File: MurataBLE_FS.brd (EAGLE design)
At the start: 90 x 63 mm, 48 parts, among them CON2 C-2395.microSD, IC1 74LVC1G00DBV, IC2 IC_DCDC_LM27313, IC3 IC_LPC11U3XQFN33, IC4 IC_LDO_XX1117_4, IC5 1265-1139-1-ND, Q1 CLOCK_CRYSTAL_4_3225, SW1 SW_TACTSW_2PP8073, SW2 SW_TACTSW_2PP8073, SW3 SW_TACTSW_2PP8073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

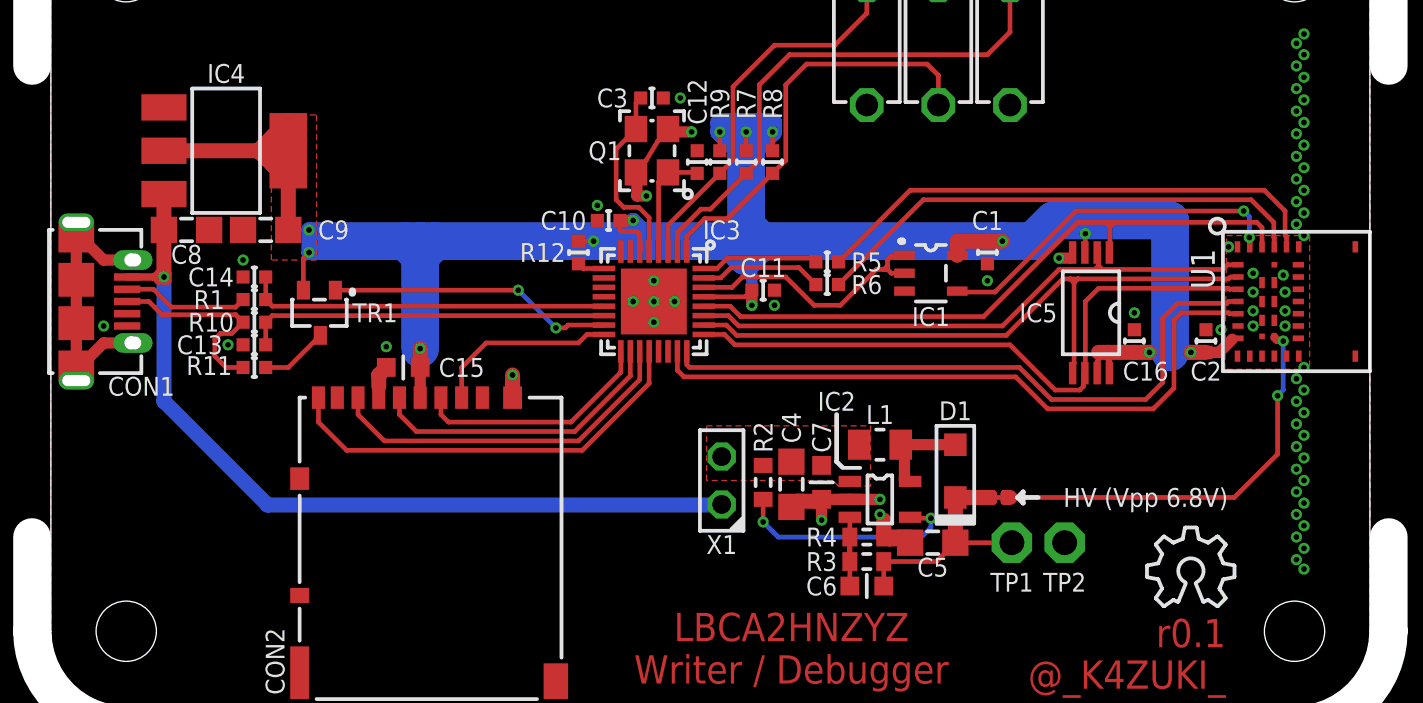
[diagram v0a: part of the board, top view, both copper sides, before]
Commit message: [ FS ] add LED1/R13/R14
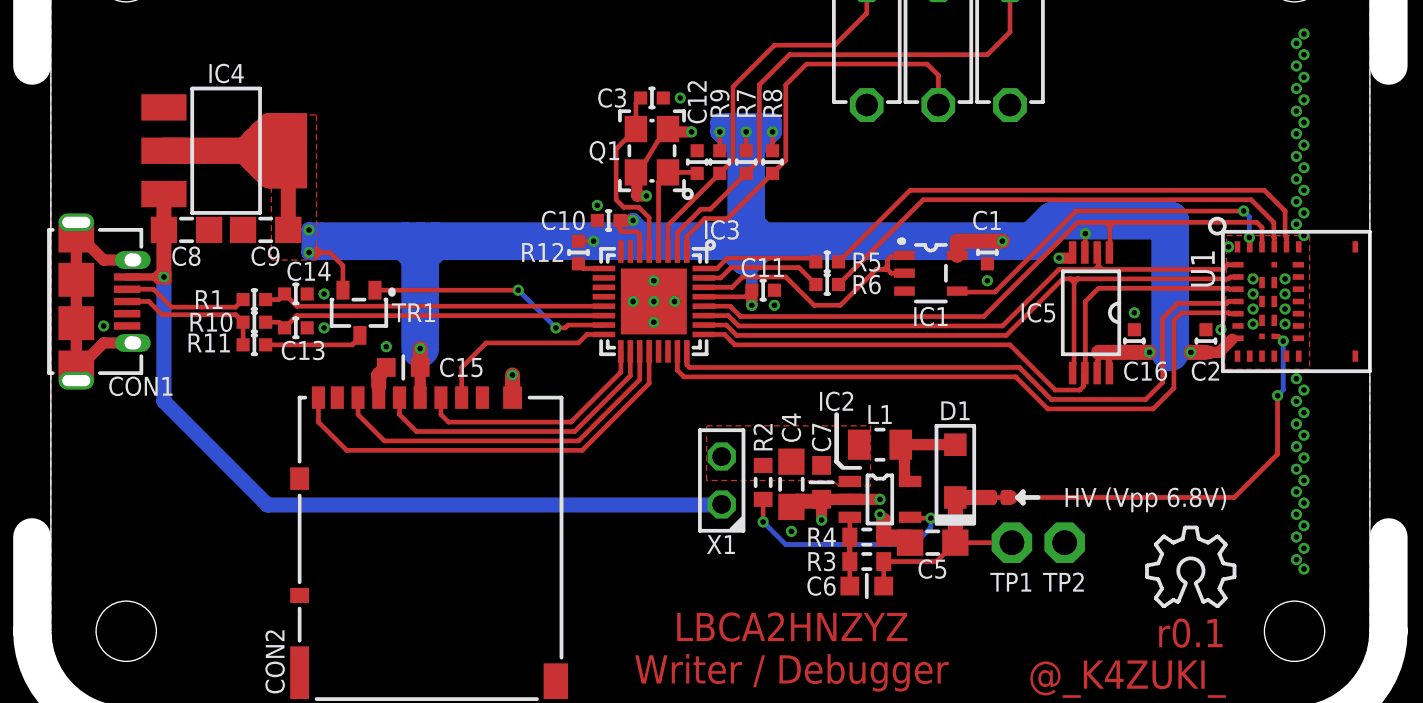
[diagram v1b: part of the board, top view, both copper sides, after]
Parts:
- moved C13 2.38 mm to (23.0, 30.1), turned to 0 degrees
- moved C14 2.38 mm to (23.0, 31.9), turned to 0 degrees
- moved TR1 2.10 mm to (26.4, 30.9)
- moved R11 1.20 mm to (20.8, 29.2)
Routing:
- net D+: track 11.1 -> 7.81 mm
- net N$12: track 15.1 -> 13.0 mm
- net N$2: track 3.60 -> 5.27 mm
- net N$20: track 19.3 -> 18.3 mm
- net N$24: track 19.3 -> 18.3 mm

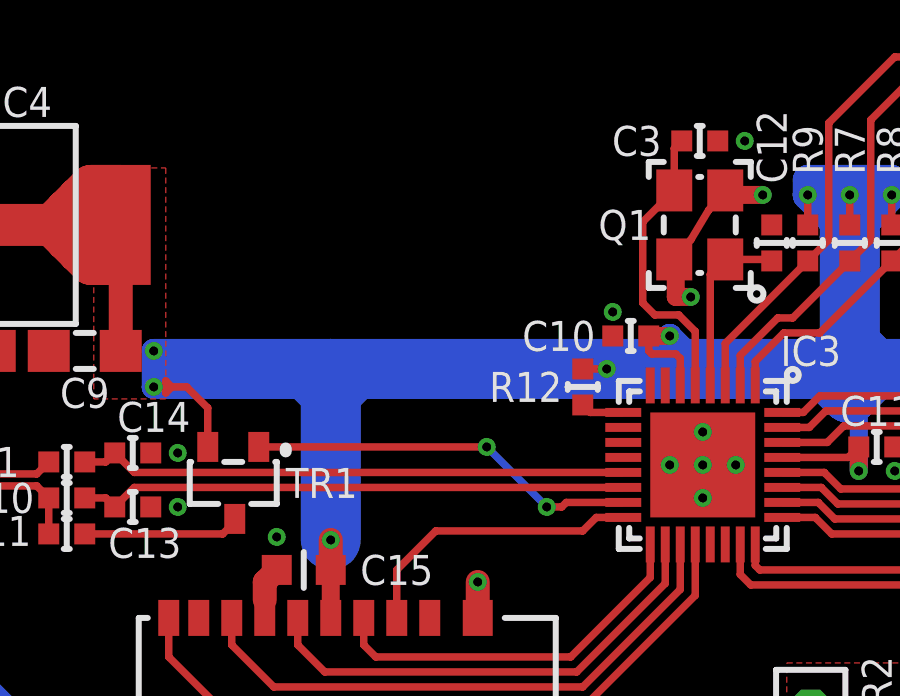
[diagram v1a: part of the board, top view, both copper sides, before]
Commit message: [ FS ] add LED1/R13/R14
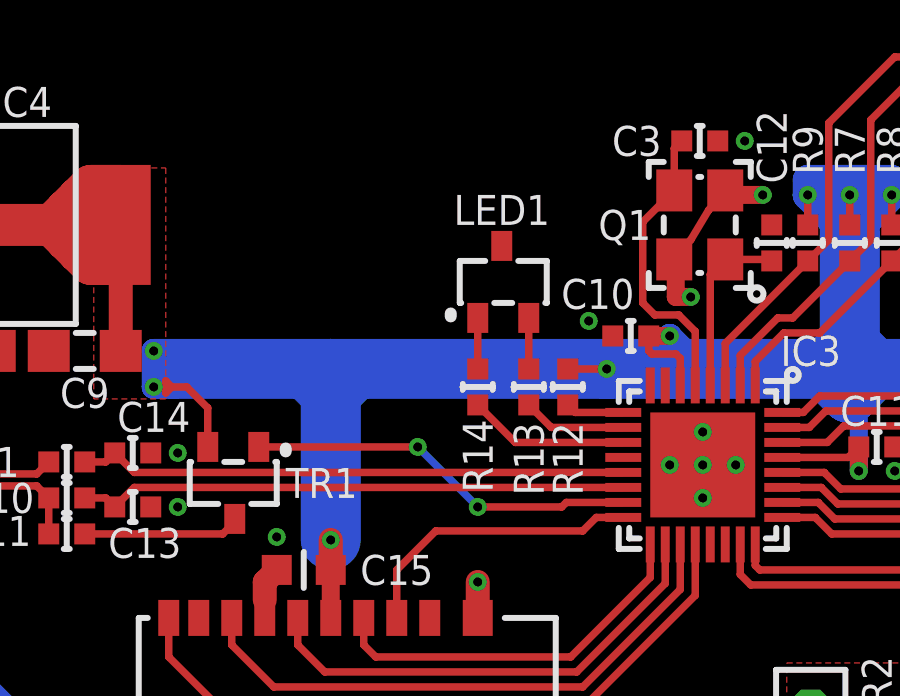
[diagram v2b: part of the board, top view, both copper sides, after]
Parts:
- added LED1: (no value), mylib:SOT95P300X140-3N
- added R13, R14: 100/1005, mylib:C0402
- moved R12 0.50 mm to (37.5, 34.1)
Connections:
- new net N$14: LED1.1, R14.2
- new net N$3: IC3.10, R13.1
- new net N$6: IC3.11, R14.1
- new net N$9: LED1.2, R13.2
- net GND: now also LED1.3
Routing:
- net N$6: track 0.00 -> 5.37 mm
- net N$3: track 0.00 -> 3.46 mm
- net N$9: track 0.00 -> 1.70 mm
- net N$14: track 0.00 -> 1.70 mm
- net N$13: track 1.45 -> 1.95 mm
- net 3.3V: track 145.4 -> 145.9 mm
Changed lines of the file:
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@@
 </element>
 <element name="C10" library="mylib" package="C0402" value="0.1u" x="39.6" y="35.8" smashed="yes" rot="R180">
-<attribute name="NAME" x="37.2" y="35.8" size="1" layer="25" font="vector" ratio="20" rot="R180" align="center"/>
+<attribute name="NAME" x="38.5" y="37.2" size="1" layer="25" font="vector" ratio="20" rot="R180" align="center"/>
 <attribute name="VALUE" x="40.2" y="37.7" size="1" layer="27" font="vector" ratio="20" rot="R180"/>
 </element>
@@
 <attribute name="VALUE" x="21.4" y="31.1" size="1" layer="27" font="vector" ratio="20" rot="R180"/>
 </element>
-<element name="R12" library="mylib" package="C0402" value="10k/1005" x="38" y="34.1" smashed="yes" rot="R270">
-<attribute name="NAME" x="36.1" y="34.1" size="1" layer="25" font="vector" ratio="20" align="center"/>
-<attribute name="VALUE" x="36.1" y="34.7" size="1" layer="27" font="vector" ratio="20" rot="R270"/>
+<element name="R12" library="mylib" package="C0402" value="10k/1005" x="37.5" y="34.1" smashed="yes" rot="R270">
+<attribute name="NAME" x="37.5" y="31.7" size="1" layer="25" font="vector" ratio="20" rot="R270" align="center"/>
+<attribute name="VALUE" x="35.6" y="34.7" size="1" layer="27" font="vector" ratio="20" rot="R270"/>
 </element>
 <element name="SW1" library="mylib" package="SW_TACTSW_P8073" value="SW_TACTSW_2PP8073" x="60.9" y="45.1" smashed="yes" rot="R90">
@@
 <attribute name="NAME" x="68.1" y="27.8" size="1" layer="25" font="vector" ratio="20" rot="R180" align="center"/>
 <attribute name="VALUE" x="69.4" y="28.8" size="1" layer="27" font="vector" ratio="20" rot="R90"/>
+</element>
+<element name="R13" library="mylib" package="C0402" value="100/1005" x="36.2" y="34.1" smashed="yes" rot="R90">
+<attribute name="NAME" x="36.2" y="31.7" size="1" layer="25" font="vector" ratio="20" rot="R270" align="center"/>
+<attribute name="VALUE" x="38.1" y="33.5" size="1" layer="27" font="vector" ratio="20" rot="R90"/>
+</element>
+<element name="R14" library="mylib" package="C0402" value="100/1005" x="34.5" y="34.1" smashed="yes" rot="R90">
+<attribute name="NAME" x="34.5" y="31.8" size="1" layer="25" font="vector" ratio="20" rot="R90" align="center"/>
+<attribute name="VALUE" x="36.4" y="33.5" size="1" layer="27" font="vector" ratio="20" rot="R90"/>
+</element>
+<element name="LED1" library="mylib" package="SOT95P300X140-3N" value="" x="35.3" y="37.6" smashed="yes">
+<attribute name="NAME" x="35.3" y="40" size="1" layer="21" font="vector" ratio="20" align="center"/>
+<attribute name="VALUE" x="35.3" y="35.1" size="1" layer="21" font="vector" ratio="20" align="center"/>
 </element>
 </elements>
@@
 <via x="43.4" y="42.3" extent="1-16" drill="0.3"/>
 <via x="44" y="40.5" extent="1-16" drill="0.3"/>
-<via x="39" y="36.6" extent="1-16" drill="0.3"/>
+<via x="38.2" y="36.3" extent="1-16" drill="0.3"/>
 <wire x1="42.75" y1="40.65" x2="42.75" y2="40.55" width="0.25" layer="1"/>
 <wire x1="42.75" y1="40.55" x2="42.2" y2="40" width="0.25" layer="1"/>
@@
 <via x="76.5" y="17.3" extent="1-16" drill="0.3"/>
 <via x="49.3" y="19.3" extent="1-16" drill="0.3"/>
+<contactref element="LED1" pad="3"/>
 </signal>
 <signal name="D-">
@@
 <wire x1="21.2" y1="40.4" x2="21.2" y2="38.6" width="1.4" layer="1"/>
 <wire x1="20.8" y1="40" x2="20.8" y2="39" width="1.4" layer="1"/>
-<wire x1="38" y1="34.7" x2="38.8" y2="34.7" width="0.25" layer="1"/>
+<wire x1="37.5" y1="34.7" x2="38.8" y2="34.7" width="0.25" layer="1"/>
 <via x="38.8" y="34.7" extent="1-16" drill="0.3"/>
 <via x="40.9" y="35.8" extent="1-16" drill="0.3"/>
@@
 <contactref element="IC3" pad="15"/>
 <wire x1="39.35" y1="30.25" x2="37.45" y2="30.25" width="0.25" layer="1"/>
-<wire x1="27.2" y1="32.1" x2="34.8" y2="32.1" width="0.25" layer="1"/>
-<via x="34.8" y="32.1" extent="1-16" drill="0.3"/>
-<wire x1="34.8" y1="32.1" x2="36.8" y2="30.1" width="0.25" layer="16"/>
-<via x="36.8" y="30.1" extent="1-16" drill="0.3"/>
-<wire x1="36.8" y1="30.1" x2="37.3" y2="30.1" width="0.25" layer="1"/>
+<wire x1="27.2" y1="32.1" x2="32.5" y2="32.1" width="0.25" layer="1"/>
+<via x="32.5" y="32.1" extent="1-16" drill="0.3"/>
+<wire x1="32.5" y1="32.1" x2="34.5" y2="30.1" width="0.25" layer="16"/>
+<via x="34.5" y="30.1" extent="1-16" drill="0.3"/>
+<wire x1="34.5" y1="30.1" x2="37.3" y2="30.1" width="0.25" layer="1"/>
 <wire x1="37.3" y1="30.1" x2="37.45" y2="30.25" width="0.25" layer="1"/>
 </signal>
@@
 <contactref element="R12" pad="2"/>
 <contactref element="IC3" pad="9"/>
-<wire x1="39.35" y1="33.25" x2="38.25" y2="33.25" width="0.25" layer="1"/>
-<wire x1="38.25" y1="33.25" x2="38" y2="33.5" width="0.25" layer="1"/>
+<wire x1="39.35" y1="33.25" x2="37.75" y2="33.25" width="0.25" layer="1"/>
+<wire x1="37.75" y1="33.25" x2="37.5" y2="33.5" width="0.25" layer="1"/>
 </signal>
 <signal name="MOSI2">
@@
 <signal name="N$1">
 </signal>
+<signal name="N$3">
+<contactref element="IC3" pad="10"/>
+<contactref element="R13" pad="1"/>
+<wire x1="39.35" y1="32.75" x2="36.95" y2="32.75" width="0.25" layer="1"/>
+<wire x1="36.95" y1="32.75" x2="36.2" y2="33.5" width="0.25" layer="1"/>
+</signal>
+<signal name="N$6">
+<contactref element="R14" pad="1"/>
+<contactref element="IC3" pad="11"/>
+<wire x1="39.35" y1="32.25" x2="35.75" y2="32.25" width="0.25" layer="1"/>
+<wire x1="34.5" y1="33.5" x2="35.75" y2="32.25" width="0.25" layer="1"/>
+</signal>
+<signal name="N$9">
+<contactref element="R13" pad="2"/>
+<contactref element="LED1" pad="2"/>
+<wire x1="36.2" y1="36.4" x2="36.2" y2="34.7" width="0.25" layer="1"/>
+</signal>
+<signal name="N$14">
+<contactref element="R14" pad="2"/>
+<contactref element="LED1" pad="1"/>
+<wire x1="34.5" y1="34.7" x2="34.5" y2="36.4" width="0.25" layer="1"/>
+</signal>
 </signals>

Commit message: [ FS ] silk move
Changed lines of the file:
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@@
 </element>
 <element name="R1" library="mylib" package="C0402" value="33/1005" x="20.8" y="31.6" smashed="yes">
-<attribute name="NAME" x="18.4" y="31.6" size="1" layer="25" font="vector" ratio="20" align="center"/>
+<attribute name="NAME" x="18.5" y="31.6" size="1" layer="25" font="vector" ratio="20" align="center"/>
 <attribute name="VALUE" x="20.2" y="29.7" size="1" layer="27" font="vector" ratio="20"/>
 </element>
@@
 </element>
 <element name="R11" library="mylib" package="C0402" value="1.5k/1005" x="20.8" y="29.2" smashed="yes" rot="R180">
-<attribute name="NAME" x="18.4" y="29.3" size="1" layer="25" font="vector" ratio="20" align="center"/>
+<attribute name="NAME" x="18.5" y="29.3" size="1" layer="25" font="vector" ratio="20" align="center"/>
 <attribute name="VALUE" x="21.4" y="31.1" size="1" layer="27" font="vector" ratio="20" rot="R180"/>
 </element>

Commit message: [ FIX ] library update
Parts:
- IC5: value 1265-1139-1-ND -> IC_MEMORY_8P__TSSOP
- Q1: value CLOCK_CRYSTAL_4_3225 -> (none)
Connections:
- net 3.3V renamed VCC
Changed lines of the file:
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@@
 <layer number="29" name="tStop" color="7" fill="3" visible="yes" active="yes"/>
 <layer number="30" name="bStop" color="7" fill="6" visible="no" active="yes"/>
-<layer number="31" name="tCream" color="7" fill="4" visible="no" active="yes"/>
+<layer number="31" name="tCream" color="7" fill="4" visible="yes" active="yes"/>
 <layer number="32" name="bCream" color="7" fill="5" visible="no" active="yes"/>
 <layer number="33" name="tFinish" color="6" fill="3" visible="no" active="yes"/>
@@
 <attribute name="VALUE" x="43.6" y="39.5" size="1" layer="27" font="vector" ratio="20" rot="R270"/>
 </element>
-<element name="Q1" library="mylib" package="CLOCK_3225" value="CLOCK_CRYSTAL_4_3225" x="41.9" y="39.5" smashed="yes" rot="R90">
+<element name="Q1" library="mylib" package="CLOCK_3225" value="" x="41.9" y="39.5" smashed="yes" rot="R90">
 <attribute name="NAME" x="39.4" y="39.5" size="1" layer="25" font="vector" ratio="20" rot="R180" align="center"/>
 </element>
@@
 <element name="U$1" library="mylib" package="ICON_OSHW" value="ICON_OSHW" x="70.5" y="17.2"/>
 <element name="U1" library="mylib" package="IC_MURATA_LBCA2HNZYZ-711" value="IC_BLE_LBCA2HNZYZ-711" x="72.4" y="35" locked="yes" rot="R270"/>
-<element name="IC5" library="mylib" package="IC_08_0.65_160MIL" value="1265-1139-1-ND" x="65.2" y="30.9" smashed="yes" rot="R180">
+<element name="IC5" library="mylib" package="IC_08_0.65_160MIL" value="IC_MEMORY_8P__TSSOP" x="65.2" y="30.9" smashed="yes" rot="R180">
 <attribute name="NAME" x="62.4" y="30.9" size="1" layer="25" font="vector" ratio="20" align="center"/>
 <attribute name="VALUE" x="62.4" y="33.5" size="1" layer="27" font="vector" ratio="20" rot="R270"/>
+<attribute name="MOUSER" value="" x="65.2" y="30.9" size="1.778" layer="27" rot="R180" display="off"/>
+<attribute name="DIGIKEY" value="1265-1184-5-ND" x="65.2" y="30.9" size="1.778" layer="27" rot="R180" display="off"/>
 </element>
 <element name="C16" library="mylib" package="C0402" value="0.1u" x="67.5" y="29.4" smashed="yes" rot="R90">
@@
 <wire x1="54.4" y1="33.4" x2="54.2" y2="33.2" width="0.25" layer="1"/>
 </signal>
-<signal name="3.3V">
+<signal name="VCC">
 <contactref element="IC1" pad="5"/>
 <contactref element="C1" pad="1"/>

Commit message: [ FS ] TP1/2; library update
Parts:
- IC5: value IC_MEMORY_8P__TSSOP -> IC_MEMORY_8P_AT25XE011_TSSOP
- PCB1: device dp_pcb:DP7043_V1 -> dp_pcb_local:DP7043_V1
- TP1: value TPPAD1-13 -> P7592
- TP2: value TPPAD1-13 -> P7591
- moved PCB1 41.1 mm to (10.0, 10.0)
- moved TP2 0.70 mm to (64.5, 18.7)
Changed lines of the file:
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@@
 <rectangle x1="76.8" y1="10" x2="80" y2="28" layer="42"/>
 <rectangle x1="59.8" y1="20.7" x2="60.8" y2="21.5" layer="29"/>
+<circle x="61" y="18.7" radius="1.6" width="0.25" layer="21"/>
+<circle x="64.5" y="18.7" radius="1.6" width="0.25" layer="21"/>
 </plain>
 <attributes>
@@
 </autorouter>
 <elements>
-<element name="PCB1" library="dp_pcb" package="DP7043_V1" value="PCB_DP_RECTANGLE-43X70" x="45" y="31.5" locked="yes" smashed="yes"/>
+<element name="PCB1" library="dp_pcb_local" package="DP7043_V1" value="PCB_DP_RECTANGLE-43X70" x="10" y="10" locked="yes" smashed="yes"/>
 <element name="IC1" library="74xx-little-us_local" package="SOT23-5" value="74LVC1G00DBV" x="56.7" y="33" smashed="yes" rot="R270">
 <attribute name="NAME" x="56.7" y="30.7" size="1" layer="25" ratio="20" rot="R180" align="center"/>
@@
 <attribute name="VALUE" x="49.4" y="22" size="1.27" layer="27" font="vector" ratio="15" rot="R270" align="center"/>
 </element>
-<element name="TP1" library="testpad_local" package="P1-13" value="TPPAD1-13" x="61" y="18.7" smashed="yes" rot="R180">
+<element name="TP1" library="testpad_local" package="P1-13" value="P7592" x="61" y="18.7" smashed="yes" rot="R180">
 <attribute name="TP_SIGNAL_NAME" value="" x="62.27" y="21.24" size="1" layer="37" rot="R180"/>
-<attribute name="NAME" x="61" y="16.6" size="1" layer="25" ratio="20" rot="R180" align="center"/>
+<attribute name="NAME" x="61" y="16.4" size="1" layer="25" ratio="20" rot="R180" align="center"/>
 <attribute name="VALUE" x="61" y="18.7" size="0.0254" layer="27" rot="R180"/>
 </element>
-<element name="TP2" library="testpad_local" package="P1-13" value="TPPAD1-13" x="63.8" y="18.7" smashed="yes" rot="R180">
-<attribute name="TP_SIGNAL_NAME" value="" x="65.07" y="21.24" size="1" layer="37" rot="R180"/>
-<attribute name="NAME" x="63.8" y="16.6" size="1" layer="25" ratio="20" rot="R180" align="center"/>
-<attribute name="VALUE" x="63.8" y="18.7" size="0.0254" layer="27" rot="R180"/>
+<element name="TP2" library="testpad_local" package="P1-13" value="P7591" x="64.5" y="18.7" smashed="yes" rot="R180">
+<attribute name="TP_SIGNAL_NAME" value="" x="65.77" y="21.24" size="1" layer="37" rot="R180"/>
+<attribute name="NAME" x="64.5" y="16.4" size="1" layer="25" ratio="20" rot="R180" align="center"/>
+<attribute name="VALUE" x="64.5" y="18.7" size="0.0254" layer="27" rot="R180"/>
 </element>
 <element name="IC3" library="mylib" package="HVQFN33" value="IC_LPC11U3XQFN33" x="42" y="31.5" smashed="yes" rot="R270">
@@
 <element name="U$1" library="mylib" package="ICON_OSHW" value="ICON_OSHW" x="70.5" y="17.2"/>
 <element name="U1" library="mylib" package="IC_MURATA_LBCA2HNZYZ-711" value="IC_BLE_LBCA2HNZYZ-711" x="72.4" y="35" locked="yes" rot="R270"/>
-<element name="IC5" library="mylib" package="IC_08_0.65_160MIL" value="IC_MEMORY_8P__TSSOP" x="65.2" y="30.9" smashed="yes" rot="R180">
+<element name="IC5" library="mylib" package="IC_08_0.65_160MIL" value="IC_MEMORY_8P_AT25XE011_TSSOP" x="65.2" y="30.9" smashed="yes" rot="R180">
 <attribute name="NAME" x="62.4" y="30.9" size="1" layer="25" font="vector" ratio="20" align="center"/>
 <attribute name="VALUE" x="62.4" y="33.5" size="1" layer="27" font="vector" ratio="20" rot="R270"/>
@@
 <vertex x="72.3" y="27.9"/>
 </polygon>
-<via x="75.5" y="31.9" extent="1-16" drill="0.3"/>
-<via x="75.5" y="31.1" extent="1-16" drill="0.3"/>
+<via x="75.4" y="31.9" extent="1-16" drill="0.3"/>
+<via x="75.4" y="31.1" extent="1-16" drill="0.3"/>
 <via x="73.8" y="31.9" extent="1-16" drill="0.3"/>
 <via x="73.8" y="31.1" extent="1-16" drill="0.3"/>
@@
 <via x="72.5" y="34.4" extent="1-16" drill="0.3"/>
 <via x="73.8" y="30.3" extent="1-16" drill="0.3"/>
-<via x="75.5" y="30.3" extent="1-16" drill="0.3"/>
+<via x="75.4" y="30.3" extent="1-16" drill="0.3"/>
 <via x="73.8" y="32.7" extent="1-16" drill="0.3"/>
-<via x="75.5" y="32.7" extent="1-16" drill="0.3"/>
+<via x="75.4" y="32.7" extent="1-16" drill="0.3"/>
 <via x="76.5" y="35" extent="1-16" drill="0.3"/>
 <via x="76.5" y="36.2" extent="1-16" drill="0.3"/>
@@
 <wire x1="45.5" y1="38.3" x2="46.2" y2="39" width="0.25" layer="1"/>
 <wire x1="46.2" y1="39" x2="46.2" y2="42.9" width="0.25" layer="1"/>
-<wire x1="53.3" y1="48.275" x2="53.3" y2="46.8" width="0.25" layer="1"/>
+<wire x1="53.3" y1="48.3" x2="53.3" y2="46.8" width="0.25" layer="1"/>
 <wire x1="53.3" y1="46.8" x2="51.6" y2="45.1" width="0.25" layer="1"/>
 <wire x1="51.6" y1="45.1" x2="48.4" y2="45.1" width="0.25" layer="1"/>
@@
 <wire x1="56.5" y1="44.1" x2="50.1" y2="44.1" width="0.25" layer="1"/>
 <wire x1="50.1" y1="44.1" x2="49" y2="43" width="0.25" layer="1"/>
-<wire x1="57.1" y1="41.925" x2="57.1" y2="43.5" width="0.25" layer="1"/>
+<wire x1="57.1" y1="41.9" x2="57.1" y2="43.5" width="0.25" layer="1"/>
 <wire x1="57.1" y1="43.5" x2="56.5" y2="44.1" width="0.25" layer="1"/>
 </signal>
@@
 <wire x1="49.2" y1="44.6" x2="47.6" y2="43" width="0.25" layer="1"/>
 <wire x1="59.7" y1="44.6" x2="60.9" y2="45.8" width="0.25" layer="1"/>
-<wire x1="60.9" y1="45.8" x2="60.9" y2="48.275" width="0.25" layer="1"/>
+<wire x1="60.9" y1="45.8" x2="60.9" y2="48.3" width="0.25" layer="1"/>
 </signal>
 <signal name="N$5">
